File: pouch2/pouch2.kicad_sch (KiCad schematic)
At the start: 29 parts, among them J101 Conn_01x06_Male, J102 Conn_01x03_Male, J103 Conn_01x04_Male, U101 Pico

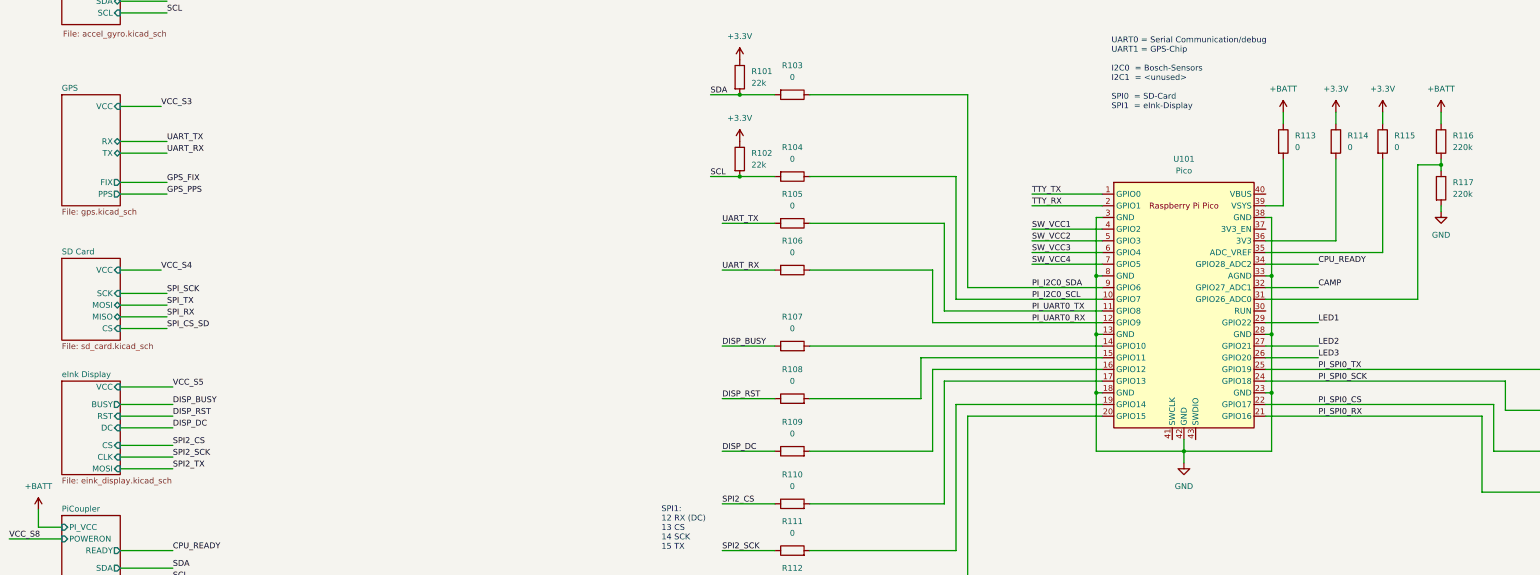
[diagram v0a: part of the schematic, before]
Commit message: updated power routing
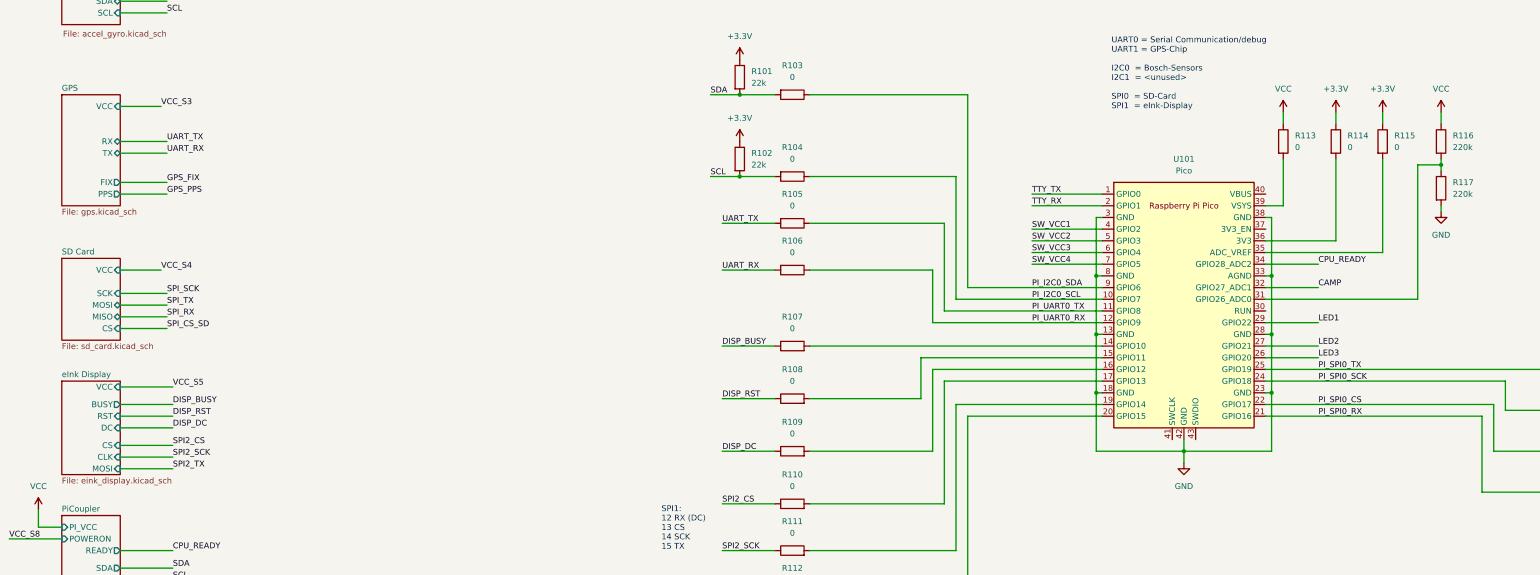
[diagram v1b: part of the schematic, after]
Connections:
- net +BATT renamed VCC

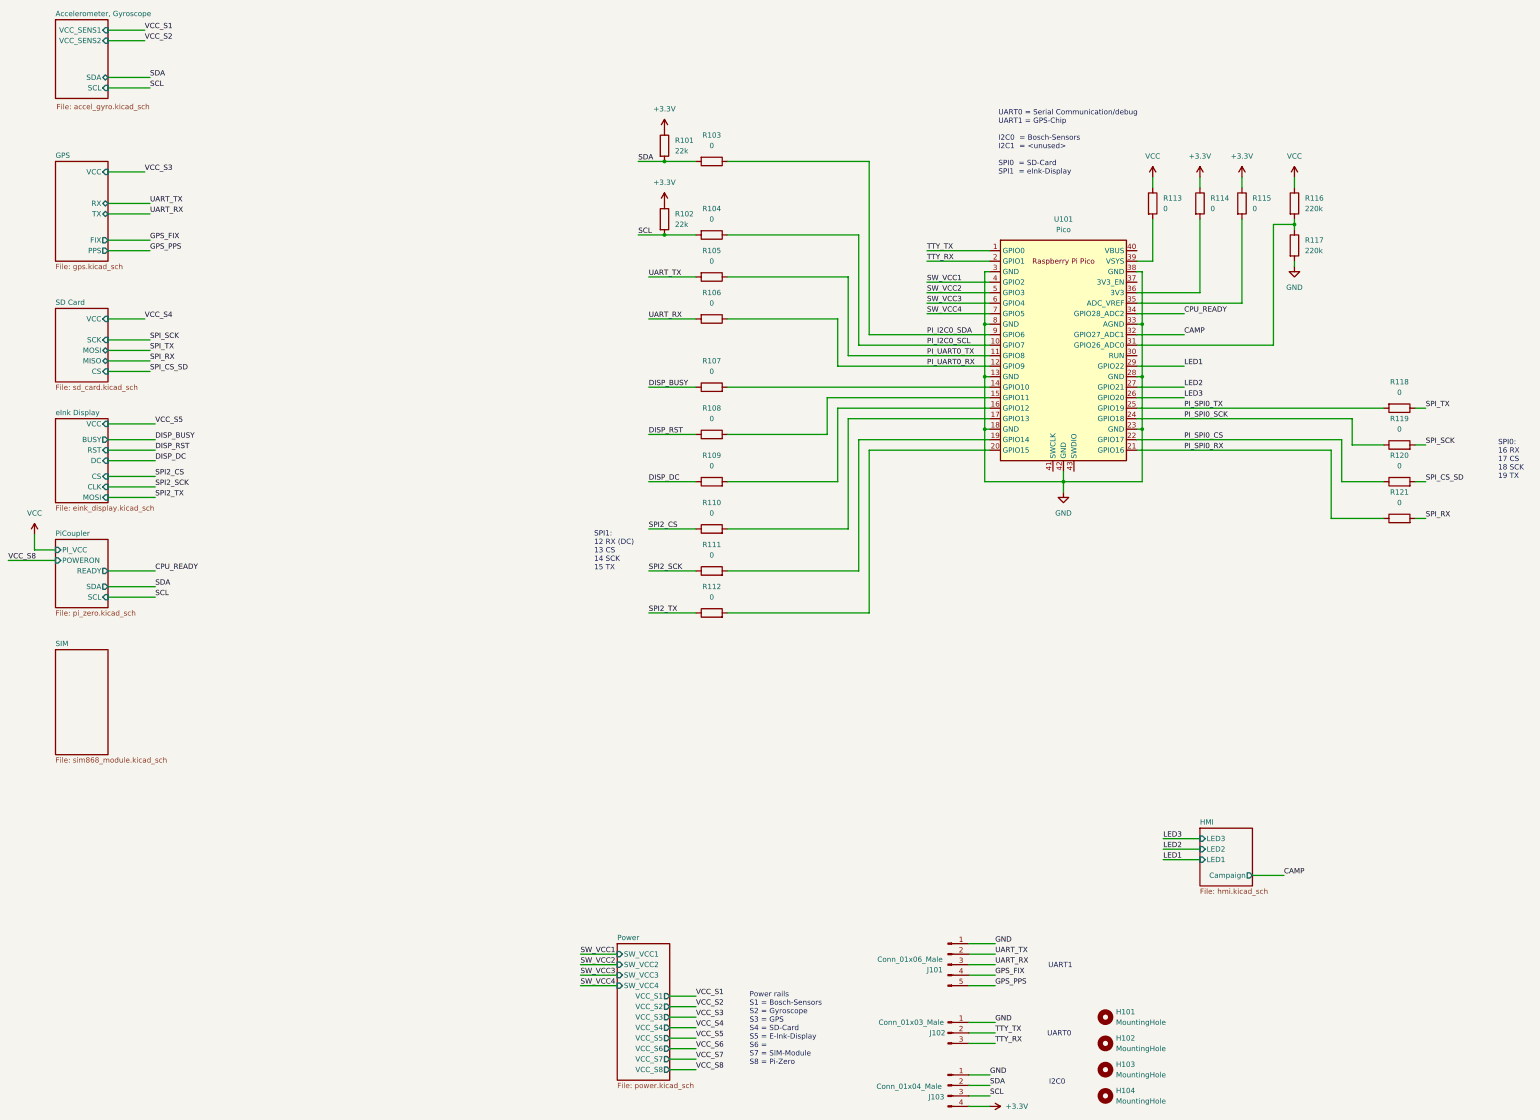
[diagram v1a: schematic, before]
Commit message: added VCC-battery measurement line
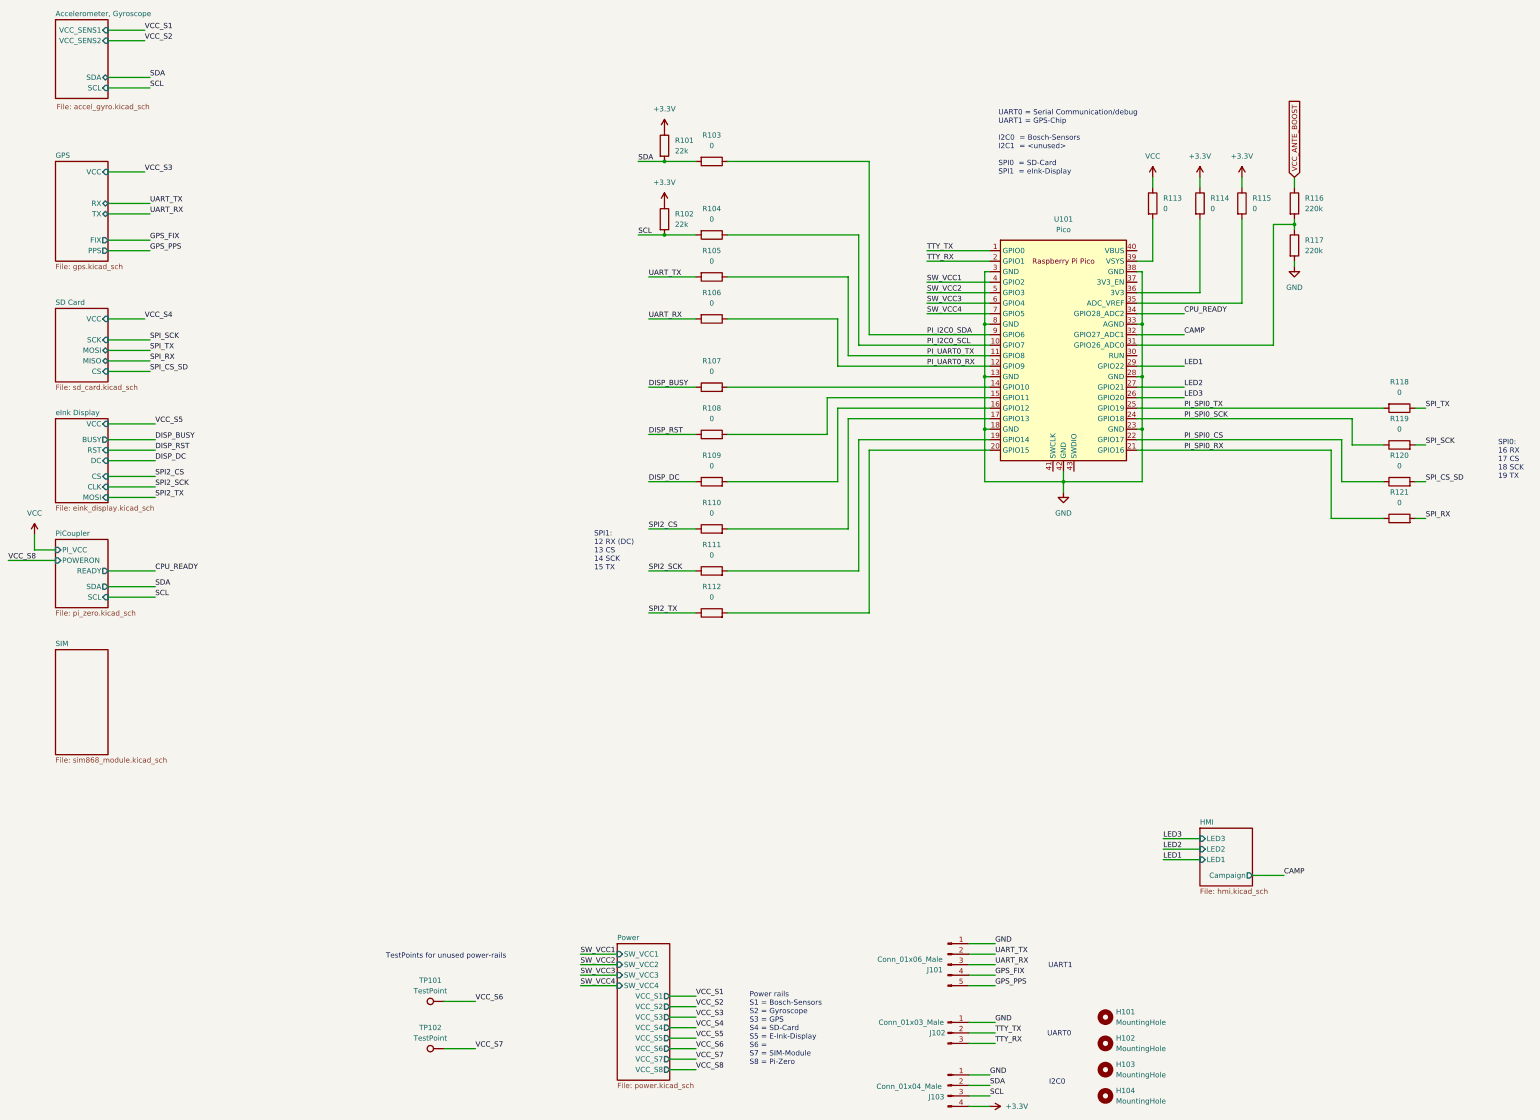
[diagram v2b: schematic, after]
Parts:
- added TP101, TP102: TestPoint, TestPoint:TestPoint_Pad_1.0x1.0mm, symbol Connector:TestPoint
- R101, R102: LCSC (none) -> C17560; MPN_Eurocircuit (none) -> GPR080522K
- R103, R104, R105, R106, R107, R108, R109, R110, R111, R112, R113, R114, R115, R118, R119, R120, R121: LCSC (none) -> C17477; MPN_Eurocircuit (none) -> GPR08050R
- R116, R117: LCSC (none) -> C17556; MPN_Eurocircuit (none) -> GPR0805220K
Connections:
- net VCC: no longer R116.1
- net VCC_S6: now also TP101.1
- net VCC_S7: now also TP102.1
- new net VCC_ANTE_BOOST: R116.1
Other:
- note added: "TestPoints for unused power-rails"

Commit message: rev1
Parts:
- H101, H102, H103, H104, TP101, TP102: OrderStatus (none) -> dnp
- J101, J102, J103, U101: OrderStatus (none) -> manual
- R101, R102, R103, R104, R105, R106, R107, R108, R109, R110, R111, R112, R113, R114, R115, R116, R117, R118, R119, R120, R121: OrderStatus (none) -> assembly
